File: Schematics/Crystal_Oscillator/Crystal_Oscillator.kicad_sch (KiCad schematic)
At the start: 4 parts

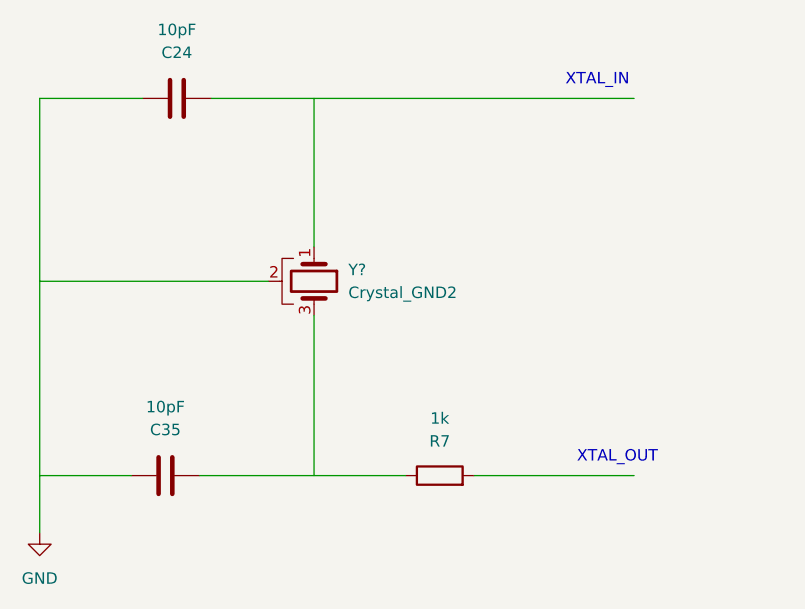
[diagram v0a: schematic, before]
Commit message: updated crystal oscillator
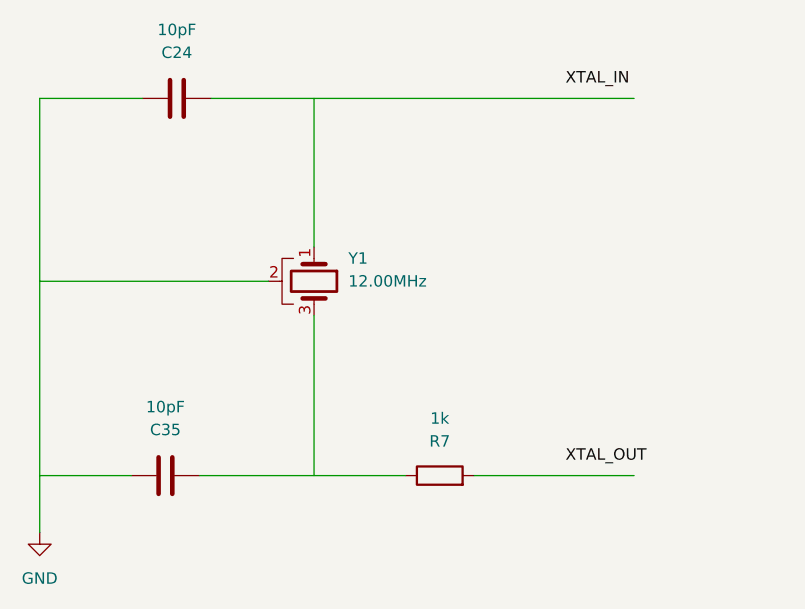
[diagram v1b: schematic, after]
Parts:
- Y1: renamed from Y?; value Crystal_GND2 -> 12.00MHz; footprint (none) -> Crystal:Crystal_SMD_2520-4Pin_2.5x2.0mm
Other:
- note removed: "XTAL_IN"
- note removed: "XTAL_OUT"
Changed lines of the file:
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@@
     (stroke (width 0) (type default) (color 0 0 0 0))
   )
-  (text "XTAL_OUT" (at 158.75 110.49 0)
+  (label "XTAL_IN" (at 157.48 68.58 0)
     (effects (font (size 1.27 1.27)) (justify left bottom))
   )
-  (text "XTAL_IN" (at 157.48 68.58 0)
+  (label "XTAL_OUT" (at 157.48 110.49 0)
     (effects (font (size 1.27 1.27)) (justify left bottom))
   )
@@
   (symbol (lib_id "Device:Crystal_GND2") (at 129.54 90.17 270) (unit 1)
     (in_bom yes) (on_board yes) (fields_autoplaced)
-    (property "Reference" "Y?" (id 0) (at 133.35 88.8999 90)
+    (property "Reference" "Y1" (id 0) (at 133.35 87.6299 90)
       (effects (font (size 1.27 1.27)) (justify left))
     )
-    (property "Value" "Crystal_GND2" (id 1) (at 133.35 91.4399 90)
+    (property "Value" "12.00MHz" (id 1) (at 133.35 90.1699 90)
       (effects (font (size 1.27 1.27)) (justify left))
     )
-    (property "Footprint" "" (id 2) (at 129.54 90.17 0)
-      (effects (font (size 1.27 1.27)) hide)
+    (property "Footprint" "Crystal:Crystal_SMD_2520-4Pin_2.5x2.0mm" (id 2) (at 133.35 92.7099 90)
+      (effects (font (size 1.27 1.27)) (justify left) hide)
     )
     (property "Datasheet" "~" (id 3) (at 129.54 90.17 0)
@@
     )
     (path "/c6a203d1-0525-4134-9b56-8d4839d12187"
-      (reference "Y?") (unit 1) (value "Crystal_GND2") (footprint "")
+      (reference "Y1") (unit 1) (value "12.00MHz") (footprint "Crystal:Crystal_SMD_2520-4Pin_2.5x2.0mm")
     )
   )

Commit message: updated crystal oscillator and flash memory on module board
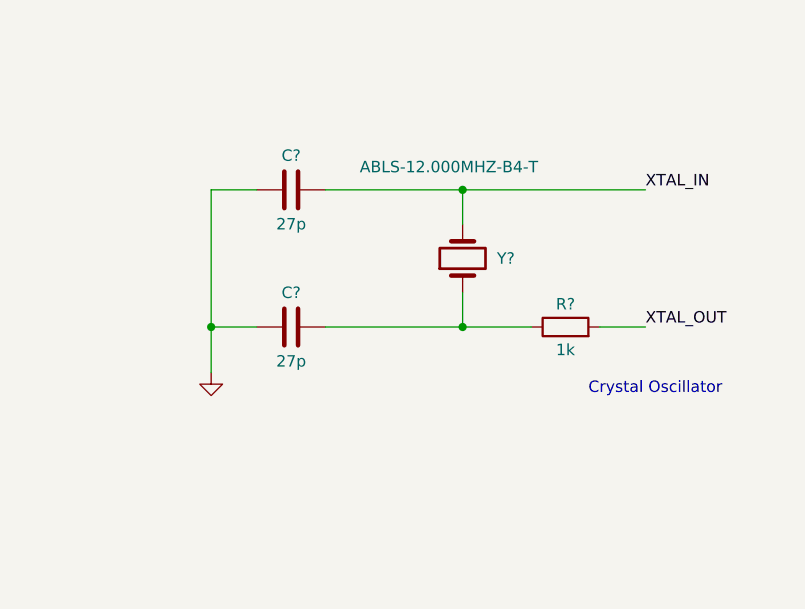
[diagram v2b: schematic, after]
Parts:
- removed 10pF: C35, symbol Device:C
- removed 10pF: C24, symbol Device:C
- removed 1k: R7, symbol Device:R
- removed Y1: 12.00MHz, Crystal:Crystal_SMD_2520-4Pin_2.5x2.0mm, symbol Device:Crystal_GND2
- added C? (x2): 27p, symbol Device:C
- added R?: 1k, symbol Device:R
- added Y?: ABLS-12.000MHZ-B4-T, symbol Device:Crystal
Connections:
- net GND: now also C?.1, C?.1
- net XTAL_IN: now also C?.2, Y?.2
- net XTAL_OUT: now also R?.2
- new net: C?.2, R?.1, Y?.1
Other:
- note added: "Crystal Oscillator"
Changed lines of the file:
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@@
 (kicad_sch (version 20211123) (generator eeschema)
   (paper "A4")
-  (wire (pts (xy 99.06 111.76) (xy 109.22 111.76))
+  (junction (at 146.05 95.25) (diameter 0) (color 0 0 0 0)
+  )
+  (junction (at 118.11 95.25) (diameter 0) (color 0 0 0 0)
+  )
+  (junction (at 146.05 80.01) (diameter 0) (color 0 0 0 0)
+  )
+  (wire (pts (xy 146.05 80.01) (xy 146.05 83.82))
     (stroke (width 0) (type default) (color 0 0 0 0))
   )
-  (wire (pts (xy 116.84 111.76) (xy 139.7 111.76))
+  (wire (pts (xy 130.81 80.01) (xy 146.05 80.01))
     (stroke (width 0) (type default) (color 0 0 0 0))
   )
-  (wire (pts (xy 147.32 111.76) (xy 165.1 111.76))
+  (wire (pts (xy 146.05 91.44) (xy 146.05 95.25))
     (stroke (width 0) (type default) (color 0 0 0 0))
   )
-  (wire (pts (xy 110.49 69.85) (xy 99.06 69.85))
+  (wire (pts (xy 130.81 95.25) (xy 146.05 95.25))
     (stroke (width 0) (type default) (color 0 0 0 0))
   )
-  (wire (pts (xy 129.54 86.36) (xy 129.54 69.85))
+  (wire (pts (xy 146.05 95.25) (xy 153.67 95.25))
     (stroke (width 0) (type default) (color 0 0 0 0))
   )
-  (wire (pts (xy 118.11 69.85) (xy 165.1 69.85))
+  (wire (pts (xy 123.19 80.01) (xy 118.11 80.01))
     (stroke (width 0) (type default) (color 0 0 0 0))
   )
-  (wire (pts (xy 99.06 90.17) (xy 124.46 90.17))
+  (wire (pts (xy 118.11 80.01) (xy 118.11 95.25))
     (stroke (width 0) (type default) (color 0 0 0 0))
   )
-  (wire (pts (xy 129.54 93.98) (xy 129.54 111.76))
+  (wire (pts (xy 161.29 95.25) (xy 166.37 95.25))
     (stroke (width 0) (type default) (color 0 0 0 0))
   )
-  (wire (pts (xy 99.06 69.85) (xy 99.06 118.11))
+  (wire (pts (xy 118.11 95.25) (xy 123.19 95.25))
     (stroke (width 0) (type default) (color 0 0 0 0))
   )
-  (label "XTAL_IN" (at 157.48 68.58 0)
+  (wire (pts (xy 146.05 80.01) (xy 166.37 80.01))
+    (stroke (width 0) (type default) (color 0 0 0 0))
+  )
+  (wire (pts (xy 118.11 95.25) (xy 118.11 100.33))
+    (stroke (width 0) (type default) (color 0 0 0 0))
+  )
+  (text "Crystal Oscillator" (at 160.02 102.87 0)
     (effects (font (size 1.27 1.27)) (justify left bottom))
   )
-  (label "XTAL_OUT" (at 157.48 110.49 0)
+  (label "XTAL_IN" (at 166.37 80.01 0)
     (effects (font (size 1.27 1.27)) (justify left bottom))
   )
-  (symbol (lib_id "power:GND") (at 99.06 118.11 0) (unit 1)
-    (in_bom yes) (on_board yes) (fields_autoplaced)
-    (property "Reference" "#PWR?" (id 0) (at 99.06 124.46 0)
+  (label "XTAL_OUT" (at 166.37 95.25 0)
+    (effects (font (size 1.27 1.27)) (justify left bottom))
+  )
+  (symbol (lib_id "Device:C") (at 127 80.01 90) (unit 1)
+    (in_bom yes) (on_board yes)
+    (property "Reference" "C?" (id 0) (at 127 76.2 90))
+    (property "Value" "27p" (id 1) (at 127 83.82 90))
+    (property "Footprint" "" (id 2) (at 130.81 79.0448 0)
       (effects (font (size 1.27 1.27)) hide)
     )
-    (property "Value" "GND" (id 1) (at 99.06 123.19 0))
-    (property "Footprint" "" (id 2) (at 99.06 118.11 0)
-      (effects (font (size 1.27 1.27)) hide)
-    )
-    (property "Datasheet" "" (id 3) (at 99.06 118.11 0)
-      (effects (font (size 1.27 1.27)) hide)
-    )
-    (pin "1")
-  )
-  (symbol (lib_id "Device:C") (at 113.03 111.76 90) (unit 1)
-    (in_bom yes) (on_board yes) (fields_autoplaced)
-    (property "Reference" "10pF" (id 0) (at 113.03 104.14 90))
-    (property "Value" "C35" (id 1) (at 113.03 106.68 90))
-    (property "Footprint" "" (id 2) (at 116.84 110.7948 0)
-      (effects (font (size 1.27 1.27)) hide)
-    )
-    (property "Datasheet" "~" (id 3) (at 113.03 111.76 0)
+    (property "Datasheet" "~" (id 3) (at 127 80.01 0)
       (effects (font (size 1.27 1.27)) hide)
     )
@@
     (pin "2")
   )
-  (symbol (lib_id "Device:R") (at 143.51 111.76 90) (unit 1)
+  (symbol (lib_id "power:GND") (at 118.11 100.33 0) (unit 1)
     (in_bom yes) (on_board yes) (fields_autoplaced)
-    (property "Reference" "1k" (id 0) (at 143.51 105.41 90))
-    (property "Value" "R7" (id 1) (at 143.51 107.95 90))
-    (property "Footprint" "" (id 2) (at 143.51 113.538 90)
+    (property "Reference" "#PWR?" (id 0) (at 118.11 106.68 0)
       (effects (font (size 1.27 1.27)) hide)
     )
-    (property "Datasheet" "~" (id 3) (at 143.51 111.76 0)
+    (property "Value" "GND" (id 1) (at 118.11 105.41 0)
+      (effects (font (size 1.27 1.27)) hide)
+    )
+    (property "Footprint" "" (id 2) (at 118.11 100.33 0)
+      (effects (font (size 1.27 1.27)) hide)
+    )
+    (property "Datasheet" "" (id 3) (at 118.11 100.33 0)
+      (effects (font (size 1.27 1.27)) hide)
+    )
+    (pin "1")
+  )
+  (symbol (lib_id "Device:Crystal") (at 146.05 87.63 90) (unit 1)
+    (in_bom yes) (on_board yes)
+    (property "Reference" "Y?" (id 0) (at 149.86 87.63 90)
+      (effects (font (size 1.27 1.27)) (justify right))
+    )
+    (property "Value" "ABLS-12.000MHZ-B4-T" (id 1) (at 134.62 77.47 90)
+      (effects (font (size 1.27 1.27)) (justify right))
+    )
+    (property "Footprint" "" (id 2) (at 146.05 87.63 0)
+      (effects (font (size 1.27 1.27)) hide)
+    )
+    (property "Datasheet" "~" (id 3) (at 146.05 87.63 0)
       (effects (font (size 1.27 1.27)) hide)
     )
@@
     (pin "2")
   )
-  (symbol (lib_id "Device:Crystal_GND2") (at 129.54 90.17 270) (unit 1)
-    (in_bom yes) (on_board yes) (fields_autoplaced)
-    (property "Reference" "Y1" (id 0) (at 133.35 87.6299 90)
-      (effects (font (size 1.27 1.27)) (justify left))
+  (symbol (lib_id "Device:C") (at 127 95.25 90) (unit 1)
+    (in_bom yes) (on_board yes)
+    (property "Reference" "C?" (id 0) (at 127 91.44 90))
+    (property "Value" "27p" (id 1) (at 127 99.06 90))
+    (property "Footprint" "" (id 2) (at 130.81 94.2848 0)
+      (effects (font (size 1.27 1.27)) hide)
     )
-    (property "Value" "12.00MHz" (id 1) (at 133.35 90.1699 90)
-      (effects (font (size 1.27 1.27)) (justify left))
-    )
-    (property "Footprint" "Crystal:Crystal_SMD_2520-4Pin_2.5x2.0mm" (id 2) (at 133.35 92.7099 90)
-      (effects (font (size 1.27 1.27)) (justify left) hide)
-    )
-    (property "Datasheet" "~" (id 3) (at 129.54 90.17 0)
+    (property "Datasheet" "~" (id 3) (at 127 95.25 0)
       (effects (font (size 1.27 1.27)) hide)
     )
     (pin "1")
     (pin "2")
-    (pin "3")
   )
-  (symbol (lib_id "Device:C") (at 114.3 69.85 90) (unit 1)
-    (in_bom yes) (on_board yes) (fields_autoplaced)
-    (property "Reference" "10pF" (id 0) (at 114.3 62.23 90))
-    (property "Value" "C24" (id 1) (at 114.3 64.77 90))
-    (property "Footprint" "" (id 2) (at 118.11 68.8848 0)
+  (symbol (lib_id "Device:R") (at 157.48 95.25 90) (unit 1)
+    (in_bom yes) (on_board yes)
+    (property "Reference" "R?" (id 0) (at 157.48 92.71 90))
+    (property "Value" "1k" (id 1) (at 157.48 97.79 90))
+    (property "Footprint" "" (id 2) (at 157.48 97.028 90)
       (effects (font (size 1.27 1.27)) hide)
     )
-    (property "Datasheet" "~" (id 3) (at 114.3 69.85 0)
+    (property "Datasheet" "~" (id 3) (at 157.48 95.25 0)
       (effects (font (size 1.27 1.27)) hide)
     )
@@
   )
   (symbol_instances
-    (path "/2a30829d-9ef7-4bc0-81ef-c2c30ac64e10"
+    (path "/86e0153d-ce3b-4c25-8543-6f03b94a2e0d"
       (reference "#PWR?") (unit 1) (value "GND") (footprint "")
     )
-    (path "/9d906019-3b24-4f0e-bcb1-e9134221a5dc"
-      (reference "1k") (unit 1) (value "R7") (footprint "")
+    (path "/35cabdc9-013a-48c2-a501-b55813cf7c81"
+      (reference "C?") (unit 1) (value "27p") (footprint "")
     )
-    (path "/8503c1c7-0041-4693-be0f-b37ef32f1b43"
-      (reference "10pF") (unit 1) (value "C35") (footprint "")
+    (path "/d1e4bba0-c1d2-4c87-b501-e07280ea97b3"
+      (reference "C?") (unit 1) (value "27p") (footprint "")
     )
-    (path "/fda0bc9f-123c-4d90-a88d-7bca4dcd3414"
-      (reference "10pF") (unit 1) (value "C24") (footprint "")
+    (path "/e273e447-c177-4284-b53e-1e47b7c6a1e5"
+      (reference "R?") (unit 1) (value "1k") (footprint "")
     )
-    (path "/c6a203d1-0525-4134-9b56-8d4839d12187"
-      (reference "Y1") (unit 1) (value "12.00MHz") (footprint "Crystal:Crystal_SMD_2520-4Pin_2.5x2.0mm")
+    (path "/97b0fd5a-b547-4890-8ed2-40c439332b8a"
+      (reference "Y?") (unit 1) (value "ABLS-12.000MHZ-B4-T") (footprint "")
     )
   )

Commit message: updated footprint for module board
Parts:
- Y?: footprint (none) -> ABLS-12:XTAL_ABLS-12.000MHZ-B4-T
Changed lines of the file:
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@@
       (effects (font (size 1.27 1.27)) (justify right))
     )
-    (property "Footprint" "" (id 2) (at 146.05 87.63 0)
+    (property "Footprint" "ABLS-12:XTAL_ABLS-12.000MHZ-B4-T" (id 2) (at 146.05 87.63 0)
       (effects (font (size 1.27 1.27)) hide)
     )
@@
     )
     (path "/97b0fd5a-b547-4890-8ed2-40c439332b8a"
-      (reference "Y?") (unit 1) (value "ABLS-12.000MHZ-B4-T") (footprint "")
+      (reference "Y?") (unit 1) (value "ABLS-12.000MHZ-B4-T") (footprint "ABLS-12:XTAL_ABLS-12.000MHZ-B4-T")
     )
   )
